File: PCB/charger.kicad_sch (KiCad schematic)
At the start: 15 parts, among them U2 BQ24072RGT

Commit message: Kleine Verbesserungen
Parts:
- R5: now not fitted; now left out of the parts list
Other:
- note added: "ILIM: maximaler Input Strom auf 1A limitiert. ISET: Charge Strom auf ~100mA gesetzt. EN2: 0; EN1: 1 => Input Strom wird durch ILIM limitiert."
- note removed: "ILIM: maximaler Input Strom auf 1A limitiert. ISET: Charge Strom auf ~100mA gesetzt."
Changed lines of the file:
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@@
 		)
 	)
-	(text "ILIM: maximaler Input Strom auf 1A limitiert.\nISET: Charge Strom auf ~100mA gesetzt."
+	(text "ILIM: maximaler Input Strom auf 1A limitiert.\nISET: Charge Strom auf ~100mA gesetzt.\nEN2: 0;  EN1: 1 \n=> Input Strom wird durch ILIM limitiert."
 		(exclude_from_sim no)
-		(at 99.06 114.3 0)
+		(at 97.282 120.142 0)
 		(effects
 			(font
@@
 		(unit 1)
 		(exclude_from_sim no)
-		(in_bom yes)
+		(in_bom no)
 		(on_board yes)
-		(dnp no)
+		(dnp yes)
 		(property "Reference" "R5"
 			(at 81.28 81.28 90)

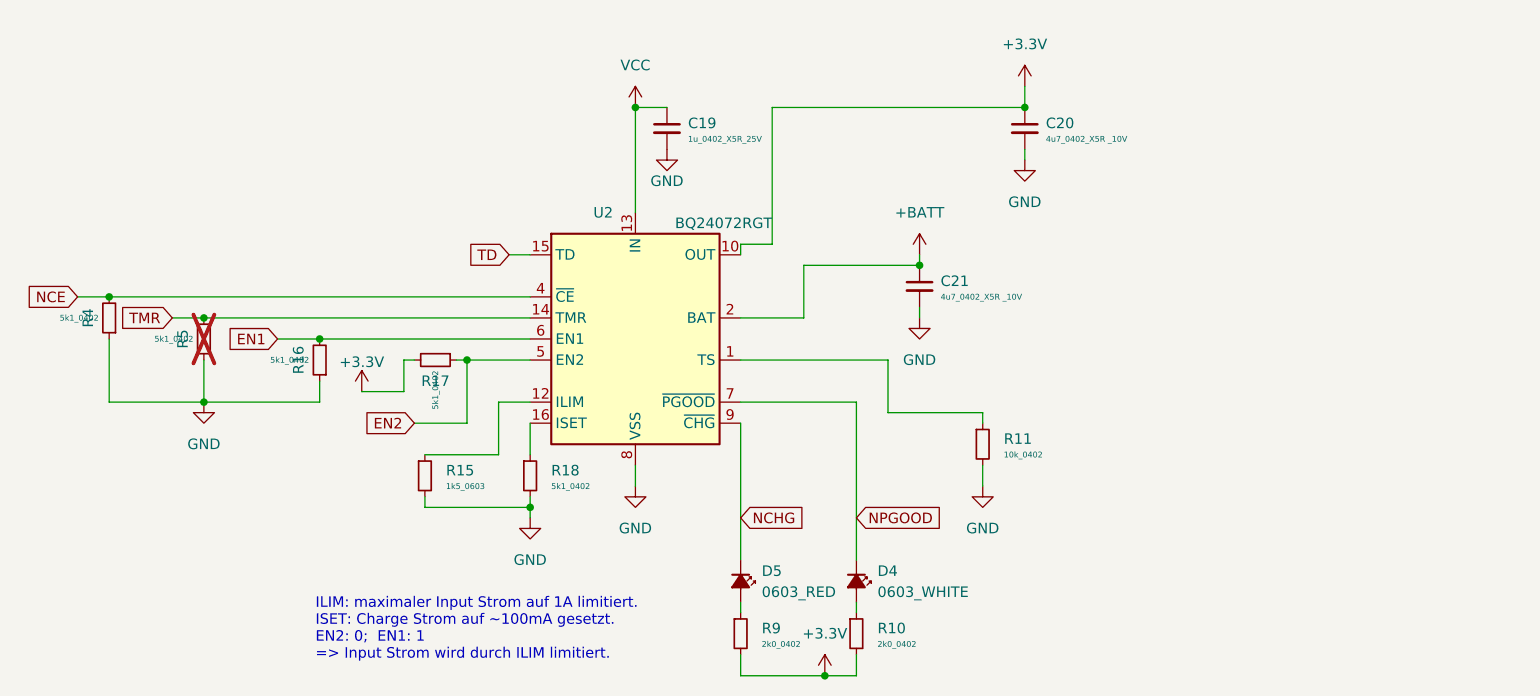
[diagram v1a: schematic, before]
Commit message: Neuer Charger IC und ein LDO
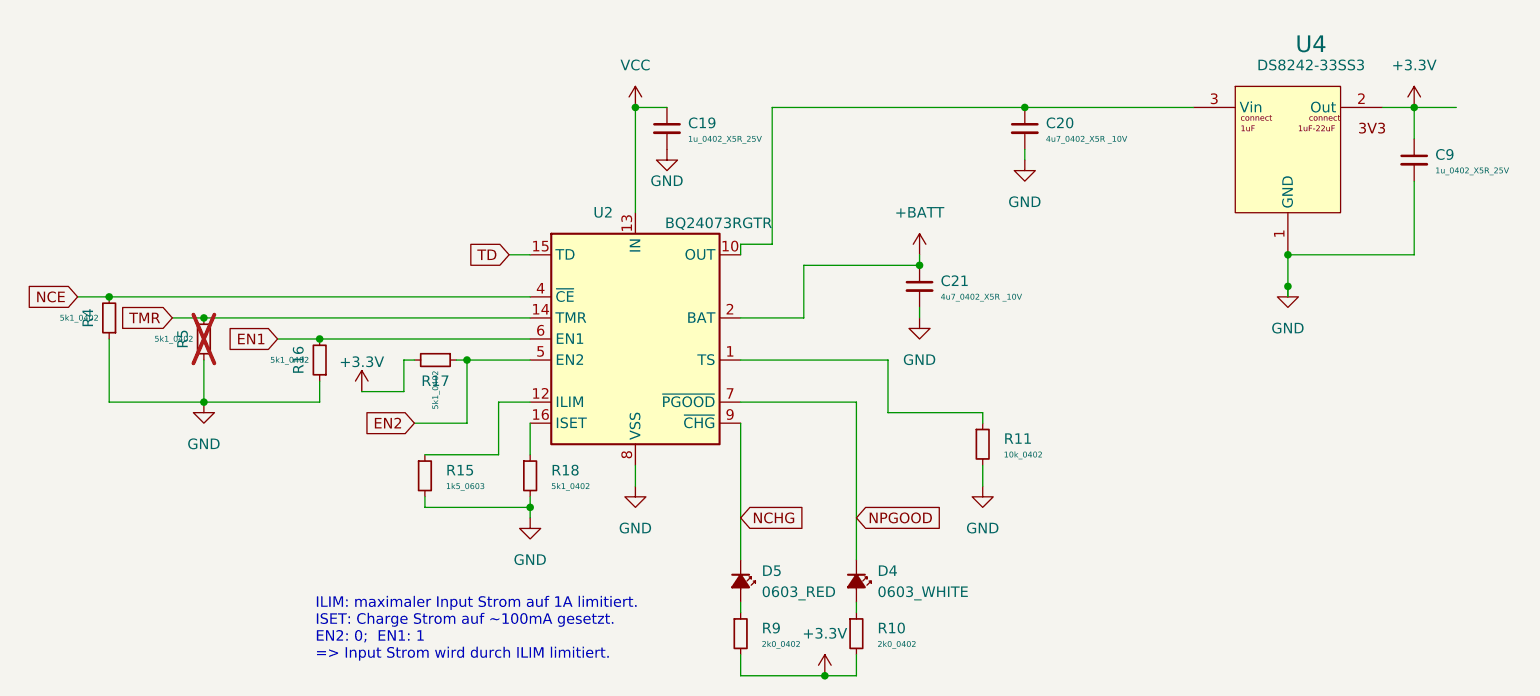
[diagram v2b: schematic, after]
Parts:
- added C9: 1u_0402_X5R_25V, Capacitor_SMD:C_0402_1005Metric, symbol capacitor_smd_standard:1u_0402_X5R_25V
- added U4: DS8242-33SS3, Package_TO_SOT_SMD:SOT-23, symbol dcdc:DS8242-33SS3(ext)
- U2: value BQ24072RGT -> BQ24073RGTR; LCSC C140288 -> C15220
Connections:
- net +3.3V: now also C9.1, U4.2 (Out); no longer C20.1, U2.10 (OUT), U2.11 (OUT)
- net GND: now also C9.2, U4.1 (GND)
- new net: C20.1, U2.10 (OUT), U2.11 (OUT), U4.3 (Vin)

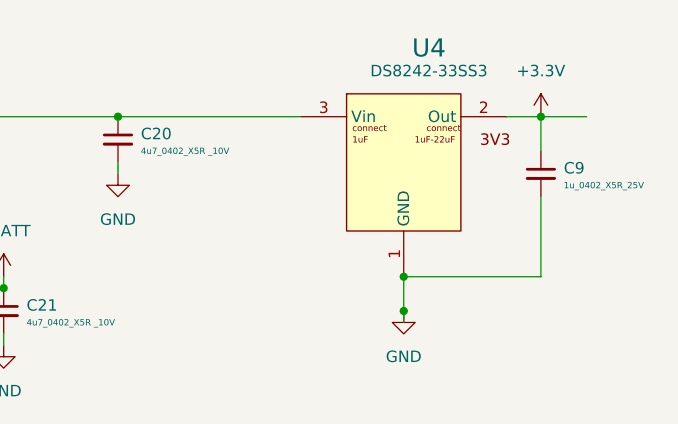
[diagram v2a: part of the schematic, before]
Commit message: LDO hinzugefügt
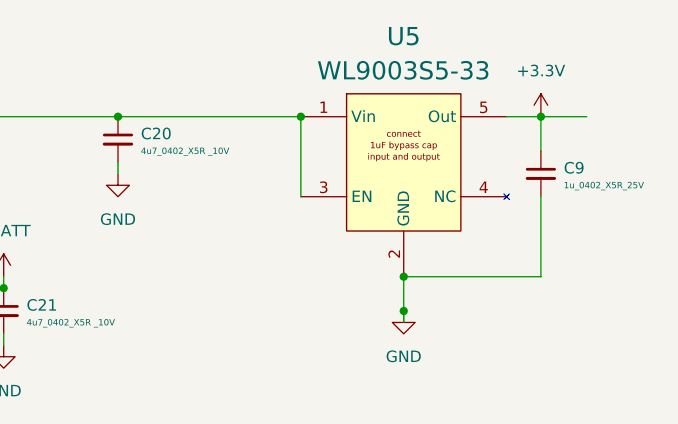
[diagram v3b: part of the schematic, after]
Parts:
- removed U4: DS8242-33SS3, Package_TO_SOT_SMD:SOT-23, symbol dcdc:DS8242-33SS3(ext)
- added U5: WL9003S5-33, Package_TO_SOT_SMD:SOT-23-5, symbol dcdc:WL9003S5-33
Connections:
- net +3.3V: now also U5.5 (Out)
- net GND: now also U5.2 (GND)
- net at C20.1, U2.10 (OUT), U2.11 (OUT): now also U5.1 (Vin), U5.3 (EN)
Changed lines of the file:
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@@
+	)
+	(junction
+		(at 214.63 71.12)
+		(diameter 0)
+		(color 0 0 0 0)
 	)
 	(junction
@@
 	)
 	(junction
-		(at 214.63 71.12)
+		(at 135.89 53.34)
 		(diameter 0)
 		(color 0 0 0 0)
 	)
 	(junction
-		(at 135.89 53.34)
+		(at 203.2 53.34)
 		(diameter 0)
 		(color 0 0 0 0)
@@
 		(pts
 			(xy 97.79 81.28) (xy 123.19 81.28)
+		)
+		(stroke
+			(width 0)
+			(type default)
+		)
+	)
+	(wire
+		(pts
+			(xy 203.2 53.34) (xy 203.2 62.23)
 		)
 		(stroke
@@
 	)
 	(symbol
+		(lib_id "dcdc:WL9003S5-33")
+		(at 214.63 58.42 0)
+		(unit 1)
+		(exclude_from_sim no)
+		(in_bom yes)
+		(on_board yes)
+		(dnp no)
+		(fields_autoplaced yes)
+		(property "Reference" "U5"
+			(at 214.63 44.45 0)
+			(effects
+				(font
+					(size 2.0066 2.0066)
+				)
+			)
+		)
+		(property "Value" "WL9003S5-33"
+			(at 214.63 48.26 0)
+			(effects
+				(font
+					(size 2.0066 2.0066)
+				)
+			)
+		)
+		(property "Footprint" "Package_TO_SOT_SMD:SOT-23-5"
+			(at 204.089 47.625 0)
+			(effects
+				(font
+					(size 2.0066 2.0066)
+				)
+				(hide yes)
+			)
+		)
+		(property "Datasheet" "https://datasheet.lcsc.com/lcsc/2102221748_WPMtek-Wei-Pan-Microelectronics-WL9003S5-33_C2688245.pdf"
+			(at 204.089 47.625 0)
+			(effects
+				(font
+					(size 2.0066 2.0066)
+				)
+				(hide yes)
+			)
+		)
+		(property "Description" " 300mA 70dB@(1kHz) 70μA 130mV Fixed 3.3V~3.3V Positive 50uVRMS 1 6.5V Uin SOT-23-5L Linear Voltage Regulators (LDO) ROHS "
+			(at 215.265 58.42 0)
+			(effects
+				(font
+					(size 1.27 1.27)
+				)
+				(hide yes)
+			)
+		)
+		(property "LCSC" "C2688245"
+			(at 215.265 58.42 0)
+			(effects
+				(font
+					(size 1.27 1.27)
+				)
+				(hide yes)
+			)
+		)
+		(pin "1"
+		)
+		(pin "3"
+		)
+		(pin "4"
+		)
+		(pin "2"
+		)
+		(pin "5"
+		)
+		(instances
+			(project ""
+				(path "/35961fef-fe97-49ba-90a9-cbb988ec3bed/fa53471f-70aa-4ce3-99ec-d97d3fb2988c"
+					(reference "U5")
+					(unit 1)
+				)
+			)
+		)
+	)
+	(symbol
 		(lib_id "resistor_smd_standard:5k1_0402")
 		(at 83.82 81.28 180)
@@
 					(unit 1)
 				)
-			)
-		)
-	)
-	(symbol
-		(lib_id "dcdc:DS8242-33SS3(ext)")
-		(at 214.63 58.42 0)
-		(unit 1)
-		(exclude_from_sim no)
-		(in_bom yes)
-		(on_board yes)
-		(dnp no)
-		(fields_autoplaced yes)
-		(property "Reference" "U4"
-			(at 217.4294 45.72 0)
-			(effects
-				(font
-					(size 2.0066 2.0066)
-				)
-			)
-		)
-		(property "Value" "DS8242-33SS3"
-			(at 217.4294 48.26 0)
-			(effects
-				(font
-					(size 1.27 1.27)
-				)
-			)
-		)
-		(property "Footprint" "Package_TO_SOT_SMD:SOT-23"
-			(at 204.089 47.625 0)
-			(effects
-				(font
-					(size 2.0066 2.0066)
-				)
-				(hide yes)
-			)
-		)
-		(property "Datasheet" "https://datasheet.lcsc.com/lcsc/2306301041_DSTECH-DS8242-33SS3_C5884134.pdf"
-			(at 204.089 47.625 0)
-			(effects
-				(font
-					(size 2.0066 2.0066)
-				)
-				(hide yes)
-			)
-		)
-		(property "Description" "500mA 70dB@(1kHz) null 3.3V positive 35V SOT-23  Linear Voltage Regulators (LDO) ROHS"
-			(at 214.63 58.42 0)
-			(effects
-				(font
-					(size 1.27 1.27)
-				)
-				(hide yes)
-			)
-		)
-		(property "LCSC" "C5884134"
-			(at 215.265 58.42 0)
-			(effects
-				(font
-					(size 1.27 1.27)
-				)
-				(hide yes)
-			)
-		)
-		(property "QtyReel" "3000"
-			(at 214.63 58.42 0)
-			(effects
-				(font
-					(size 1.27 1.27)
-				)
-				(hide yes)
-			)
-		)
-		(property "Price1000" "0.0179"
-			(at 214.63 58.42 0)
-			(effects
-				(font
-					(size 1.27 1.27)
-				)
-				(hide yes)
-			)
-		)
-		(property "JLCPCB_CORRECTION" "0;0;180"
-			(at 214.63 58.42 0)
-			(effects
-				(font
-					(size 1.27 1.27)
-				)
-				(hide yes)
-			)
-		)
-		(pin "1"
-		)
-		(pin "3"
-		)
-		(pin "2"
-		)
-		(instances
-			(project ""
-				(path "/35961fef-fe97-49ba-90a9-cbb988ec3bed/fa53471f-70aa-4ce3-99ec-d97d3fb2988c"
-					(reference "U4")
-					(unit 1)
-				)
